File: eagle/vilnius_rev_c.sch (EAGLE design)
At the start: 43 parts, among them IC1 PIC18F2580, IC3 MCP2551SN, IC4 LM2575S, IC5 MCP604, J1 OSTTE-12, J2 A00-108-220-450, Q1 10 MHz

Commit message: Main functionality in place
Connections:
- net GND: now also IC5P.V-
- net VCC: now also IC5P.V+
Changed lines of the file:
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@@
 <part name="R107" library="rcl" deviceset="R-EU_" device="R0805" value="10K"/>
 <part name="GND29" library="SUPPLY1" deviceset="GND" device=""/>
+<part name="P+2" library="SUPPLY1" deviceset="VCC" device=""/>
+<part name="GND18" library="SUPPLY1" deviceset="GND" device=""/>
 </parts>
 <sheets>
@@
 <instance part="R107" gate="G$1" x="116.84" y="63.5" rot="R90"/>
 <instance part="GND29" gate="1" x="116.84" y="55.88"/>
+<instance part="P+2" gate="VCC" x="60.96" y="63.5"/>
+<instance part="GND18" gate="1" x="60.96" y="35.56"/>
+<instance part="IC5" gate="P" x="60.96" y="48.26"/>
 </instances>
 <busses>
@@
 <pinref part="P+13" gate="VCC" pin="VCC"/>
 </segment>
+<segment>
+<pinref part="IC5" gate="P" pin="V+"/>
+<pinref part="P+2" gate="VCC" pin="VCC"/>
+<wire x1="60.96" y1="55.88" x2="60.96" y2="60.96" width="0.1524" layer="91"/>
+</segment>
 </net>
 <net name="GND" class="0">
@@
 <pinref part="GND29" gate="1" pin="GND"/>
 </segment>
-</net>
+<segment>
+<pinref part="IC5" gate="P" pin="V-"/>
+<pinref part="GND18" gate="1" pin="GND"/>
+<wire x1="60.96" y1="40.64" x2="60.96" y2="38.1" width="0.1524" layer="91"/>
+</segment>
+</net>

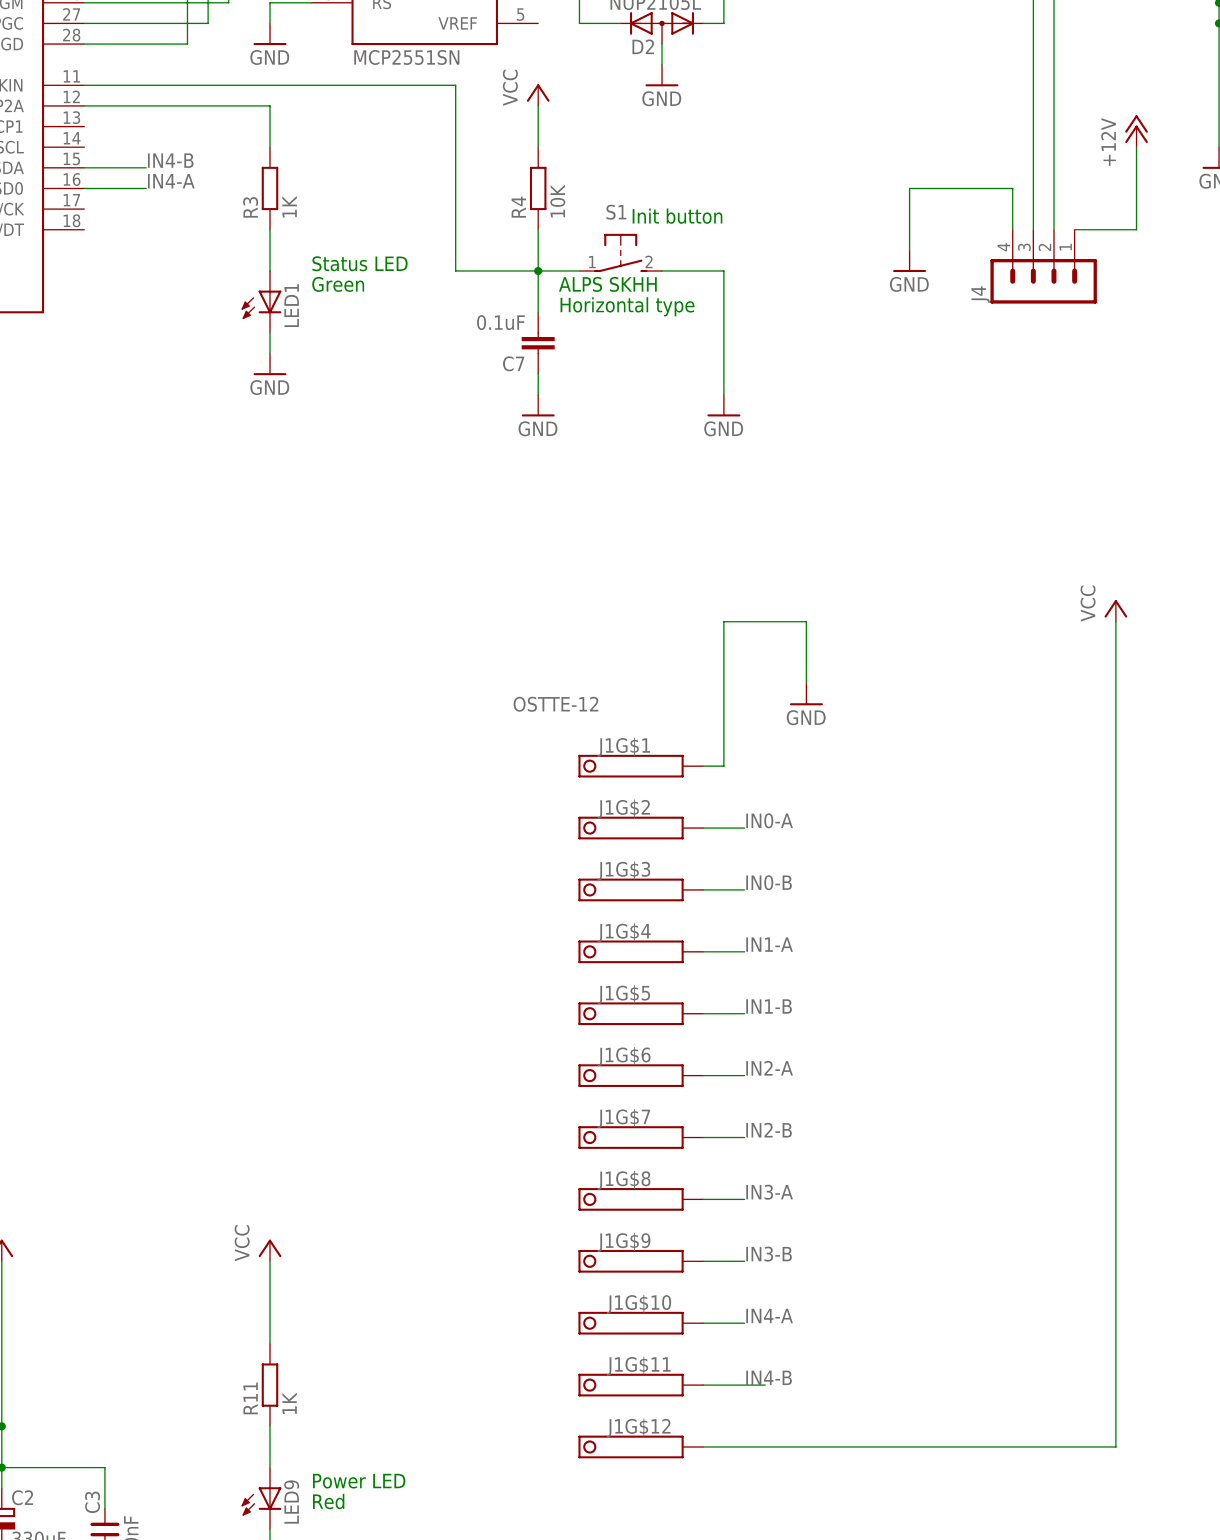
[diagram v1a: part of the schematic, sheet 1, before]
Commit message: I/O event handling in place
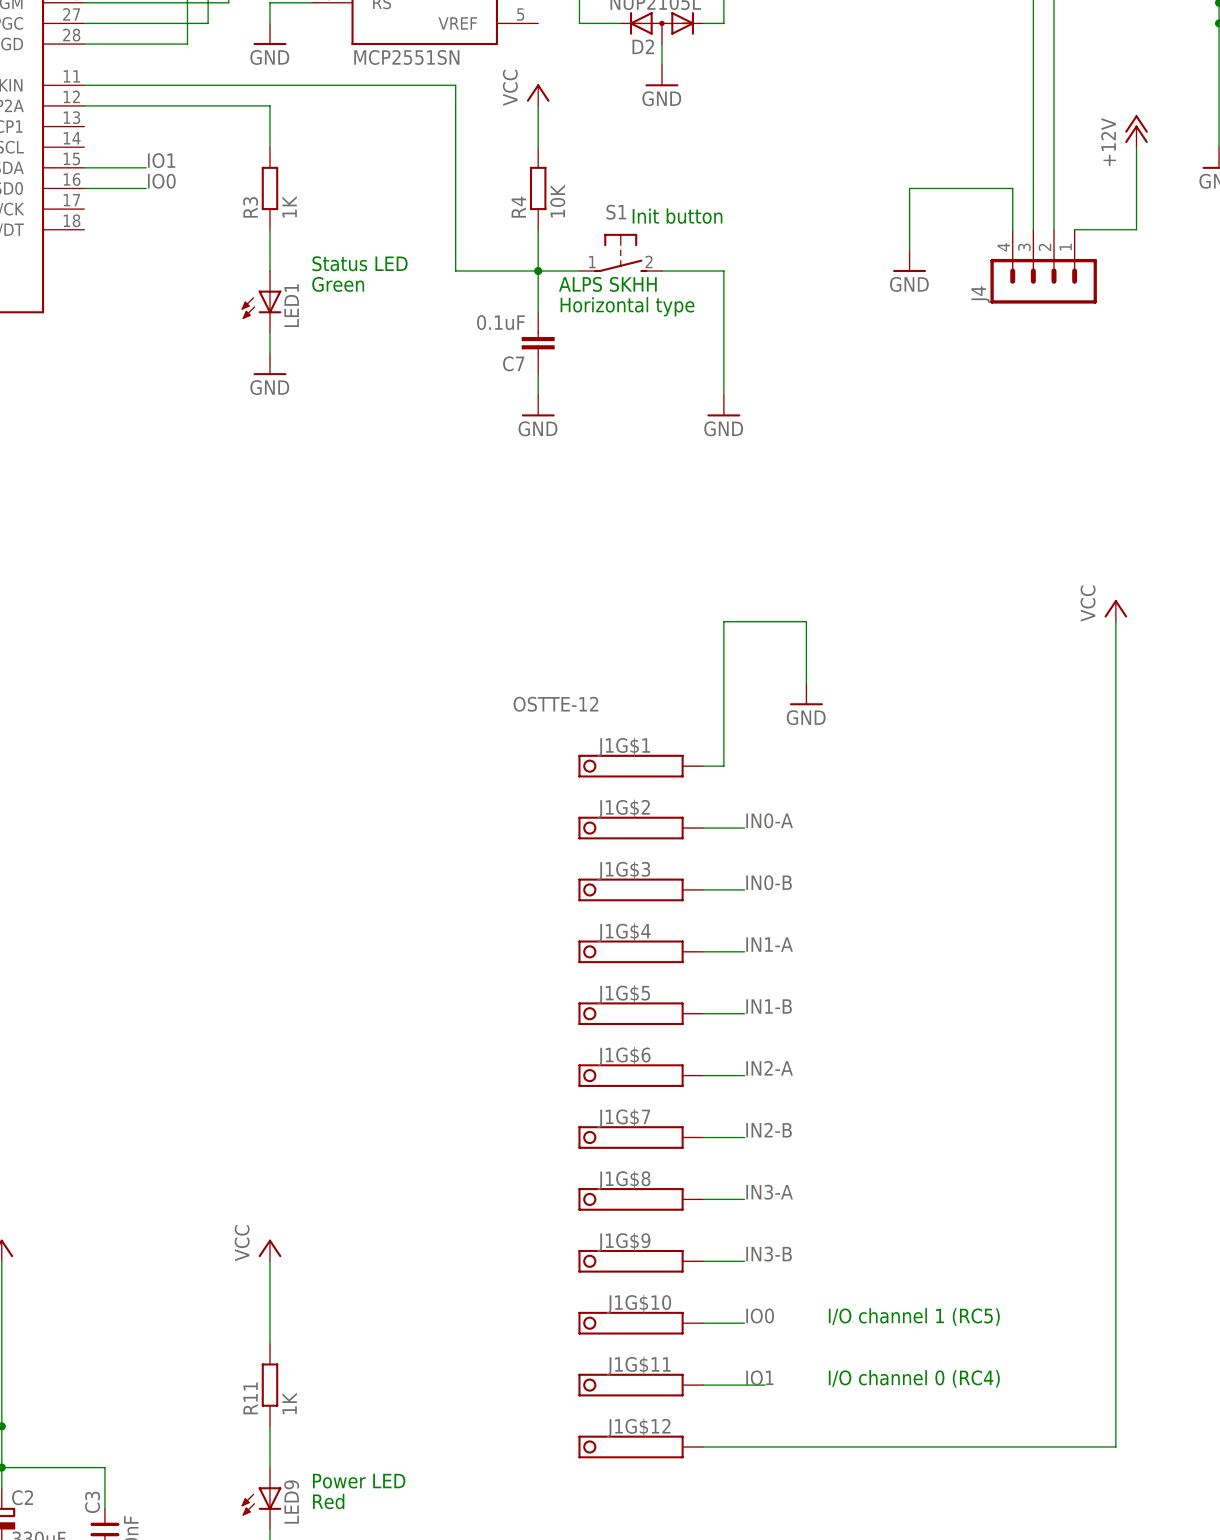
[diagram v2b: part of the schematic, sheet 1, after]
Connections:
- net IN4-A renamed IO0
- net IN4-B renamed IO1
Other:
- note added: "Channel 0 (RA3)"
- note added: "Channel 1 (RA2)"
- note added: "Channel 2 (RA1)"
- note added: "Channel 3 (RA0)"
- note added: "I/O channel 0 (RC4)"
- note added: "I/O channel 1 (RC5)"
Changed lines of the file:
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@@
 <text x="231.14" y="251.46" size="1.778" layer="91">termination</text>
 <text x="231.14" y="259.08" size="1.778" layer="91">R17</text>
+<text x="233.68" y="43.18" size="1.778" layer="91">I/O channel 0 (RC4)</text>
+<text x="233.68" y="50.8" size="1.778" layer="91">I/O channel 1 (RC5)</text>
 </plain>
 <instances>
@@
 </segment>
 </net>
-<net name="IN4-A" class="0">
-<segment>
-<wire x1="218.44" y1="50.8" x2="223.52" y2="50.8" width="0.1524" layer="91"/>
-<label x="223.52" y="50.8" size="1.778" layer="95"/>
-<pinref part="J1" gate="G$10" pin="K"/>
-</segment>
-<segment>
-<wire x1="142.24" y1="190.5" x2="149.86" y2="190.5" width="0.1524" layer="91"/>
-<label x="149.86" y="190.5" size="1.778" layer="95"/>
-<pinref part="IC1" gate="G$1" pin="RC5/SD0"/>
-</segment>
-</net>
-<net name="IN4-B" class="0">
-<segment>
-<wire x1="218.44" y1="43.18" x2="226.06" y2="43.18" width="0.1524" layer="91"/>
-<label x="223.52" y="43.18" size="1.778" layer="95"/>
-<pinref part="J1" gate="G$11" pin="K"/>
-</segment>
-<segment>
-<wire x1="142.24" y1="193.04" x2="149.86" y2="193.04" width="0.1524" layer="91"/>
-<label x="149.86" y="193.04" size="1.778" layer="95"/>
-<pinref part="IC1" gate="G$1" pin="RC4/SDI/SDA"/>
-</segment>
-</net>
 <net name="CANL" class="0">
 <segment>
@@
 </segment>
 </net>
+<net name="IO0" class="0">
+<segment>
+<wire x1="218.44" y1="50.8" x2="223.52" y2="50.8" width="0.1524" layer="91"/>
+<label x="223.52" y="50.8" size="1.778" layer="95"/>
+<pinref part="J1" gate="G$10" pin="K"/>
+</segment>
+<segment>
+<wire x1="142.24" y1="190.5" x2="149.86" y2="190.5" width="0.1524" layer="91"/>
+<label x="149.86" y="190.5" size="1.778" layer="95"/>
+<pinref part="IC1" gate="G$1" pin="RC5/SD0"/>
+</segment>
+</net>
+<net name="IO1" class="0">
+<segment>
+<wire x1="218.44" y1="43.18" x2="226.06" y2="43.18" width="0.1524" layer="91"/>
+<label x="223.52" y="43.18" size="1.778" layer="95"/>
+<pinref part="J1" gate="G$11" pin="K"/>
+</segment>
+<segment>
+<wire x1="142.24" y1="193.04" x2="149.86" y2="193.04" width="0.1524" layer="91"/>
+<label x="149.86" y="193.04" size="1.778" layer="95"/>
+<pinref part="IC1" gate="G$1" pin="RC4/SDI/SDA"/>
+</segment>
+</net>
 </nets>
 </sheet>
 <sheet>
 <plain>
+<text x="139.7" y="132.08" size="1.778" layer="91">Channel 0 (RA3)</text>
+<text x="139.7" y="116.84" size="1.778" layer="91">Channel 1 (RA2)</text>
+<text x="139.7" y="96.52" size="1.778" layer="91">Channel 2 (RA1)</text>
+<text x="139.7" y="73.66" size="1.778" layer="91">Channel 3 (RA0)</text>
 </plain>
 <instances>

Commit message: Changed value of C14 to 10uF
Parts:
- C8: value 1 uF -> 10 uF
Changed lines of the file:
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@@
 <part name="LED9" library="led" deviceset="LED" device="CHIP-LED0805"/>
 <part name="P+9" library="SUPPLY1" deviceset="VCC" device=""/>
-<part name="C8" library="rcl" deviceset="C-EU" device="C0805" value="1 uF"/>
+<part name="C8" library="rcl" deviceset="C-EU" device="C0805" value="10 uF"/>
 <part name="GND2" library="SUPPLY1" deviceset="GND" device=""/>
 <part name="R17" library="rcl" deviceset="R-EU_" device="R0805" value="120"/>
